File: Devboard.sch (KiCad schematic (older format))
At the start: 35 parts, among them J1 Power, J10 terminal, J2 Left, J3 ARM-JTAG, J4 Right, J5 JTAG, J6 Screw_Terminal_01x02, J7 Jack-DC, J8 Power, J9 DNP, Q1 IRF7101, SW1 RESET, U1 TRADFRI, U2 AMS1117-3.3

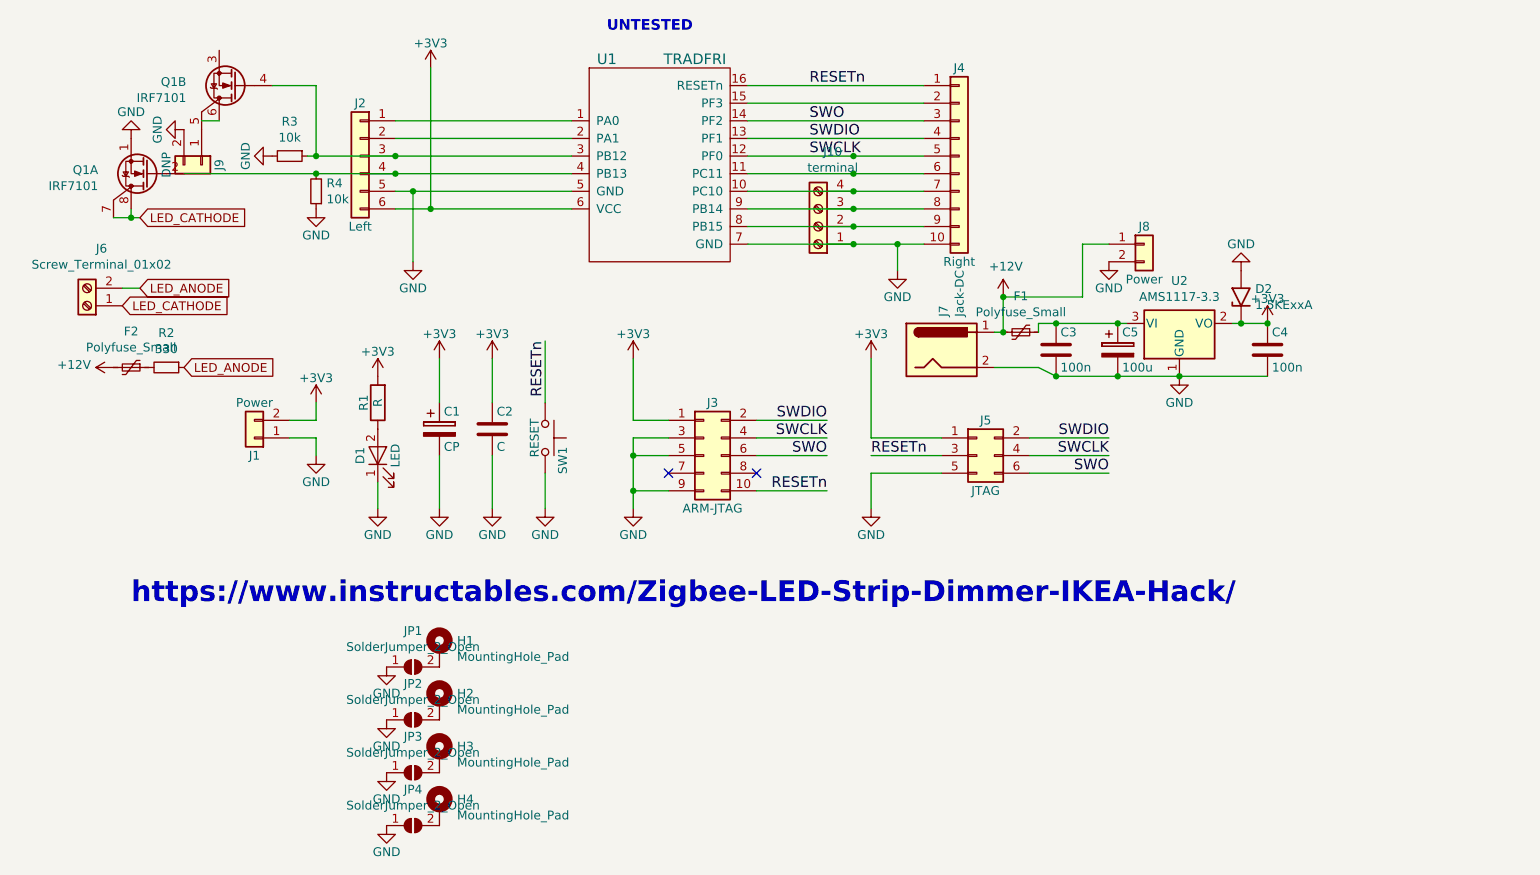
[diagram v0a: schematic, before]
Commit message: schematic texts and minor stylishing
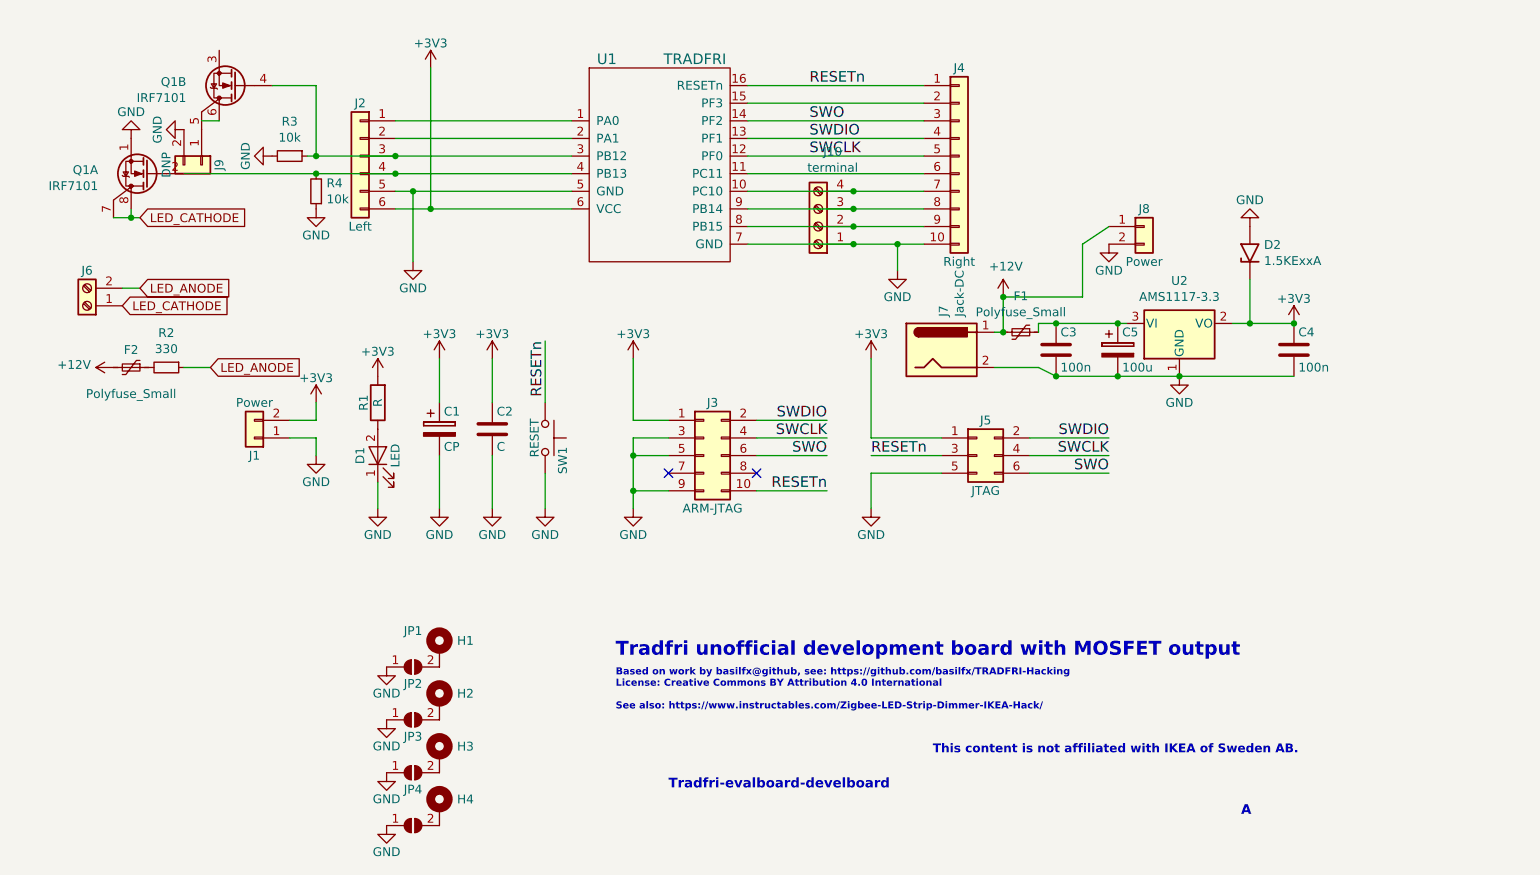
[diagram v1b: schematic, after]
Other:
- note added: "A"
- note added: "Based on work by basilfx@github, see: https://github.com/basilfx/TRADFRI-Hacking\nLicense: Creative Commons BY Attribution 4.0 International\n\nSee also: https://www.instructables.com/Zigbee-LED-Strip-Dimmer-IKEA-Hack/"
- note added: "This content is not affiliated with IKEA of Sweden AB."
- note added: "Tradfri unofficial development board with MOSFET output"
- note added: "Tradfri-evalboard-develboard"
- note removed: "UNTESTED"
- note removed: "https://www.instructables.com/Zigbee-LED-Strip-Dimmer-IKEA-Hack/"
- moved on the sheet: C4, D2, J8
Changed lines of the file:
@@
 Text Label 6500 3250 2    60   ~ 0
 SWO
-Text Notes 3650 750  0    60   ~ 12
-UNTESTED
 Wire Wire Line
 	6050 3250 6500 3250
@@
 P 2700 4250
 F 0 "H1" H 2800 4299 50  0000 L CNN
-F 1 "MountingHole_Pad" H 2800 4208 50  0000 L CNN
+F 1 "MountingHole_Pad" H 2800 4208 50  0001 L CNN
 F 2 "MountingHole:MountingHole_3.5mm_Pad_TopBottom" H 2700 4250 50  0001 C CNN
 F 3 "~" H 2700 4250 50  0001 C CNN
@@
 P 2700 4550
 F 0 "H2" H 2800 4599 50  0000 L CNN
-F 1 "MountingHole_Pad" H 2800 4508 50  0000 L CNN
+F 1 "MountingHole_Pad" H 2800 4508 50  0001 L CNN
 F 2 "MountingHole:MountingHole_3.5mm_Pad_TopBottom" H 2700 4550 50  0001 C CNN
 F 3 "~" H 2700 4550 50  0001 C CNN
@@
 P 2700 4850
 F 0 "H3" H 2800 4899 50  0000 L CNN
-F 1 "MountingHole_Pad" H 2800 4808 50  0000 L CNN
+F 1 "MountingHole_Pad" H 2800 4808 50  0001 L CNN
 F 2 "MountingHole:MountingHole_3.5mm_Pad_TopBottom" H 2700 4850 50  0001 C CNN
 F 3 "~" H 2700 4850 50  0001 C CNN
@@
 P 2700 5150
 F 0 "H4" H 2800 5199 50  0000 L CNN
-F 1 "MountingHole_Pad" H 2800 5108 50  0000 L CNN
+F 1 "MountingHole_Pad" H 2800 5108 50  0001 L CNN
 F 2 "MountingHole:MountingHole_3.5mm_Pad_TopBottom" H 2700 5150 50  0001 C CNN
 F 3 "~" H 2700 5150 50  0001 C CNN
@@
 L Devboard-rescue:C C4
 U 1 1 6097B587
-P 7400 2550
-F 0 "C4" H 7425 2650 50  0000 L CNN
-F 1 "100n" H 7425 2450 50  0000 L CNN
-F 2 "Capacitor_SMD:C_0805_2012Metric_Pad1.18x1.45mm_HandSolder" H 7438 2400 50  0001 C CNN
-F 3 "" H 7400 2550 50  0001 C CNN
-	1    7400 2550
-	1    0    0    -1
-$EndComp
-Wire Wire Line
-	7200 2400 7250 2400
+P 7550 2550
+F 0 "C4" H 7575 2650 50  0000 L CNN
+F 1 "100n" H 7575 2450 50  0000 L CNN
+F 2 "Capacitor_SMD:C_0805_2012Metric_Pad1.18x1.45mm_HandSolder" H 7588 2400 50  0001 C CNN
+F 3 "" H 7550 2550 50  0001 C CNN
+	1    7550 2550
+	1    0    0    -1
+$EndComp
+Wire Wire Line
+	7200 2400 7300 2400
 Connection ~ 6200 2700
 Connection ~ 6900 2700
 Wire Wire Line
-	6900 2700 7400 2700
+	6900 2700 7550 2700
 $Comp
 L Devboard-rescue:+3V3 #PWR0102
 U 1 1 609894C4
-P 7400 2400
-F 0 "#PWR0102" H 7400 2250 50  0001 C CNN
-F 1 "+3V3" H 7400 2540 50  0000 C CNN
-F 2 "" H 7400 2400 50  0001 C CNN
-F 3 "" H 7400 2400 50  0001 C CNN
-	1    7400 2400
-	1    0    0    -1
-$EndComp
-Connection ~ 7400 2400
+P 7550 2400
+F 0 "#PWR0102" H 7550 2250 50  0001 C CNN
+F 1 "+3V3" H 7550 2540 50  0000 C CNN
+F 2 "" H 7550 2400 50  0001 C CNN
+F 3 "" H 7550 2400 50  0001 C CNN
+	1    7550 2400
+	1    0    0    -1
+$EndComp
+Connection ~ 7550 2400
 Wire Wire Line
 	6100 2650 6200 2700
@@
 	6100 2400 6100 2450
 Connection ~ 6200 2400
-Text Notes 950  4000 0    118  ~ 24
-https://www.instructables.com/Zigbee-LED-Strip-Dimmer-IKEA-Hack/
+Text Notes 3700 4600 0    40   ~ 8
+Based on work by basilfx@github, see: https://github.com/basilfx/TRADFRI-Hacking\nLicense: Creative Commons BY Attribution 4.0 International\n\nSee also: https://www.instructables.com/Zigbee-LED-Strip-Dimmer-IKEA-Hack/
 $Comp
 L Devboard-rescue:CP C5
@@
 L Diode:1.5KExxA D2
 U 1 1 60A825BC
-P 7250 2250
-F 0 "D2" V 7296 2170 50  0000 R CNN
-F 1 "1.5KExxA" V 7205 2170 50  0000 R CNN
-F 2 "Diode_SMD:D_SMB_Handsoldering" H 7250 2050 50  0001 C CNN
-F 3 "https://www.vishay.com/docs/88301/15ke.pdf" H 7200 2250 50  0001 C CNN
-	1    7250 2250
+P 7300 2000
+F 0 "D2" V 7346 1920 50  0000 R CNN
+F 1 "1.5KExxA" V 7255 1920 50  0000 R CNN
+F 2 "Diode_SMD:D_SMB_Handsoldering" H 7300 1800 50  0001 C CNN
+F 3 "https://www.vishay.com/docs/88301/15ke.pdf" H 7250 2000 50  0001 C CNN
+	1    7300 2000
 	0    -1   -1   0
 $EndComp
-Connection ~ 7250 2400
-Wire Wire Line
-	7250 2400 7400 2400
 $Comp
 L Devboard-rescue:GND #PWR0104
 U 1 1 60A83B7F
-P 7250 2100
-F 0 "#PWR0104" H 7250 1850 50  0001 C CNN
-F 1 "GND" H 7250 1950 50  0000 C CNN
-F 2 "" H 7250 2100 50  0001 C CNN
-F 3 "" H 7250 2100 50  0001 C CNN
-	1    7250 2100
+P 7300 1850
+F 0 "#PWR0104" H 7300 1600 50  0001 C CNN
+F 1 "GND" H 7300 1700 50  0000 C CNN
+F 2 "" H 7300 1850 50  0001 C CNN
+F 3 "" H 7300 1850 50  0001 C CNN
+	1    7300 1850
 	-1   0    0    1
 $EndComp
@@
 U 1 1 60A6BA34
 P 950 2650
-F 0 "F2" V 745 2650 50  0000 C CNN
-F 1 "Polyfuse_Small" V 836 2650 50  0000 C CNN
+F 0 "F2" V 850 2650 50  0000 C CNN
+F 1 "Polyfuse_Small" V 1100 2650 50  0000 C CNN
 F 2 "Resistor_THT:R_Axial_DIN0207_L6.3mm_D2.5mm_P10.16mm_Horizontal" H 1000 2450 50  0001 L CNN
 F 3 "~" H 950 2650 50  0001 C CNN
@@
 L Devboard-rescue:Conn_01x02 J8
 U 1 1 60AEAEA6
-P 6700 1950
-F 0 "J8" H 6700 2050 50  0000 C CNN
-F 1 "Power" H 6700 1750 50  0000 C CNN
-F 2 "Connector_PinHeader_2.54mm:PinHeader_1x02_P2.54mm_Vertical" H 6700 1950 50  0001 C CNN
-F 3 "" H 6700 1950 50  0001 C CNN
-	1    6700 1950
+P 6700 1850
+F 0 "J8" H 6700 1950 50  0000 C CNN
+F 1 "Power" H 6700 1650 50  0000 C CNN
+F 2 "Connector_PinHeader_2.54mm:PinHeader_1x02_P2.54mm_Vertical" H 6700 1850 50  0001 C CNN
+F 3 "" H 6700 1850 50  0001 C CNN
+	1    6700 1850
 	1    0    0    -1
 $EndComp
@@
 L Devboard-rescue:GND #PWR0107
 U 1 1 60AF08D3
-P 6500 2050
-F 0 "#PWR0107" H 6500 1800 50  0001 C CNN
-F 1 "GND" H 6500 1900 50  0000 C CNN
-F 2 "" H 6500 2050 50  0001 C CNN
-F 3 "" H 6500 2050 50  0001 C CNN
-	1    6500 2050
-	1    0    0    -1
-$EndComp
-Wire Wire Line
-	6500 1950 6350 1950
+P 6500 1950
+F 0 "#PWR0107" H 6500 1700 50  0001 C CNN
+F 1 "GND" H 6500 1800 50  0000 C CNN
+F 2 "" H 6500 1950 50  0001 C CNN
+F 3 "" H 6500 1950 50  0001 C CNN
+	1    6500 1950
+	1    0    0    -1
+$EndComp
+Wire Wire Line
+	6500 1850 6350 1950
 Wire Wire Line
 	6350 1950 6350 2250
@@
 U 1 1 6097D02D
 P 700 2300
-F 0 "J6" H 618 1975 50  0000 C CNN
-F 1 "Screw_Terminal_01x02" H 618 2066 50  0000 C CNN
+F 0 "J6" H 700 2100 50  0000 C CNN
+F 1 "Screw_Terminal_01x02" H 618 2066 50  0001 C CNN
 F 2 "TerminalBlock_Phoenix:TerminalBlock_Phoenix_MKDS-1,5-2_1x02_P5.00mm_Horizontal" H 700 2300 50  0001 C CNN
 F 3 "~" H 700 2300 50  0001 C CNN
@@
 	0    -1   -1   0
 $EndComp
-Text GLabel 1250 2650 2    50   Input ~ 0
+Text GLabel 1400 2650 2    50   Input ~ 0
 LED_ANODE
 $Comp
@@
 Wire Wire Line
 	4450 1850 5050 1850
-Wire Wire Line
-	4450 1550 5050 1550
 $Comp
 L Connector:Screw_Terminal_01x04 J10
@@
 	-1   0    0    1
 $EndComp
-Connection ~ 5050 1550
-Wire Wire Line
-	5050 1550 5450 1550
 Connection ~ 5050 1650
 Wire Wire Line
@@
 Wire Wire Line
 	5050 1950 5300 1950
-Wire Wire Line
-	4450 1450 5050 1450
-Connection ~ 5050 1450
-Wire Wire Line
-	5050 1450 5450 1450
 $Comp
 L Jumper:SolderJumper_2_Open JP1
@@
 P 2550 4350
 F 0 "JP1" H 2550 4555 50  0000 C CNN
-F 1 "SolderJumper_2_Open" H 2550 4464 50  0000 C CNN
+F 1 "SolderJumper_2_Open" H 2550 4464 50  0001 C CNN
 F 2 "Jumper:SolderJumper-2_P1.3mm_Open_RoundedPad1.0x1.5mm" H 2550 4350 50  0001 C CNN
 F 3 "~" H 2550 4350 50  0001 C CNN
@@
 P 2550 4650
 F 0 "JP2" H 2550 4855 50  0000 C CNN
-F 1 "SolderJumper_2_Open" H 2550 4764 50  0000 C CNN
+F 1 "SolderJumper_2_Open" H 2550 4764 50  0001 C CNN
 F 2 "Jumper:SolderJumper-2_P1.3mm_Open_RoundedPad1.0x1.5mm" H 2550 4650 50  0001 C CNN
 F 3 "~" H 2550 4650 50  0001 C CNN
@@
 P 2550 4950
 F 0 "JP3" H 2550 5155 50  0000 C CNN
-F 1 "SolderJumper_2_Open" H 2550 5064 50  0000 C CNN
+F 1 "SolderJumper_2_Open" H 2550 5064 50  0001 C CNN
 F 2 "Jumper:SolderJumper-2_P1.3mm_Open_RoundedPad1.0x1.5mm" H 2550 4950 50  0001 C CNN
 F 3 "~" H 2550 4950 50  0001 C CNN
@@
 P 2550 5250
 F 0 "JP4" H 2550 5455 50  0000 C CNN
-F 1 "SolderJumper_2_Open" H 2550 5364 50  0000 C CNN
+F 1 "SolderJumper_2_Open" H 2550 5364 50  0001 C CNN
 F 2 "Jumper:SolderJumper-2_P1.3mm_Open_RoundedPad1.0x1.5mm" H 2550 5250 50  0001 C CNN
 F 3 "~" H 2550 5250 50  0001 C CNN
@@
 	1    0    0    -1
 $EndComp
+Wire Wire Line
+	4450 1550 5450 1550
+Wire Wire Line
+	4450 1450 5450 1450
+Text Notes 3700 4300 0    79   ~ 16
+Tradfri unofficial development board with MOSFET output
+Wire Wire Line
+	7300 2400 7300 2150
+Connection ~ 7300 2400
+Wire Wire Line
+	7300 2400 7550 2400
+Wire Wire Line
+	1400 2650 1250 2650
+Text Notes 7250 5200 0    55   ~ 11
+A
+Text Notes 4000 5050 0    55   ~ 11
+Tradfri-evalboard-develboard
+Text Notes 5500 4850 0    50   ~ 10
+This content is not affiliated with IKEA of Sweden AB.
 $EndSCHEMATC

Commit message: enhancements to pcb, this will be possible rev B
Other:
- note added: "B"
- note removed: "A"
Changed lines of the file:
@@
 	1400 2650 1250 2650
 Text Notes 7250 5200 0    55   ~ 11
-A
+B
 Text Notes 4000 5050 0    55   ~ 11
 Tradfri-evalboard-develboard
